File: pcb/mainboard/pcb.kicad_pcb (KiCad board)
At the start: 2 copper layers, 227 x 50 mm, 396 parts, among them J301 Conn_02x05_Odd_Even, J401 MICRO_SD(TFC-WPAPR-08), J501 Conn_01x40_MountingPin, J502 Conn_01x06_MountingPin, J503 Conn_01x40_MountingPin, J504 Conn_01x28_MountingPin, J601 USB_A, J602 USB_A, J603 USB_C_Receptacle_USB2.0, J604 USB_B_Micro, J701 Conn_01x02, J702 Conn_01x02, J703 AudioJack3_SwitchT, J800 Conn_01x28_MountingPin, Q1 FDMC8327L, Q2 FDMC8327L, Q3 2SK3018, U1 SY8120, U101 MCIMX7S5EVM08SC, U2 SY8120, U202 MT41K256M16HA, U203 MT41K256M16HA, U3 SY8120, U301 LPC5500_FBD64, U302 74LS154, U4 SY8120, U5 SY8120, U501 CAT4139, U502 SSD2828, U503 DS90C385A, U504 SM351LT, U6 SY8120, U601 USB2514B_Bi, U602 AP2171W, U603 AP2171W, U604 FUSB302BMPX, U605 USBLC6-2P6, U606 CP2102N-Axx-xQFN28, U7 LT8606, U701 WM8960, U8 LTC4162-F, U9 ADP123, U901 RTL8723BS, Y101 24MHz, Y102 32.768kHz, Y301 16MHz, Y501 24MHz, Y601 24MHz

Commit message: - pcb: components placed
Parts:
- removed C615, C616: 100nF, Capacitor_SMD:C_0402_1005Metric
- removed C617, C618: 10uF/6.3V, Capacitor_SMD:C_0603_1608Metric
- removed C701, C702, C703, C704: 1uF, Capacitor_SMD:C_0402_1005Metric
- removed D301: 1N5819, Diode_SMD:D_SOD-123
- removed D601, D602: LED, LED_SMD:LED_0603_1608Metric
- removed MK701, MK702: Microphone, Connector_PinSocket_1.27mm:PinSocket_1x02_P1.27mm_Vertical
- removed R303, R609, TH1: 10K, Resistor_SMD:R_0402_1005Metric
- removed R608: 100K, Resistor_SMD:R_0402_1005Metric
- removed R610: 20K, Resistor_SMD:R_0402_1005Metric
- removed R701, R702: 2.2K, Resistor_SMD:R_0402_1005Metric
- removed U606: CP2102N-Axx-xQFN28, Package_DFN_QFN:QFN-28-1EP_5x5mm_P0.5mm_EP3.35x3.35mm
- added C317: 100nF, Capacitor_SMD:C_0402_1005Metric, F.Cu at (99.1, 100.8)
- added C619: 10uF/6.3V, Capacitor_SMD:C_0603_1608Metric, F.Cu at (246.7, 97.3)
- added C620: 10uF/6.3V, Capacitor_SMD:C_0603_1608Metric, F.Cu at (246.5, 118.7)
- added C76: 220nF, Capacitor_SMD:C_0402_1005Metric, B.Cu at (144.3, 95.8)
- added C77: 2.2uF, Capacitor_SMD:C_0402_1005Metric, B.Cu at (142.2, 93.5)
- added C78: 220nF, Capacitor_SMD:C_0402_1005Metric, B.Cu at (143.8, 97.5)
- added C79: 220nF, Capacitor_SMD:C_0402_1005Metric, B.Cu at (144.1, 99.2)
- added C80: 2.2uF, Capacitor_SMD:C_0402_1005Metric, B.Cu at (145.2, 98.8)
- added C81: 1uF, Capacitor_SMD:C_0402_1005Metric, F.Cu at (63.5, 104.4)
- added J1: Conn_01x10_MountingPin, Connector_FFC-FPC:Hirose_FH12-10S-0.5SH_1x10-1MP_P0.50mm_Horizontal, F.Cu at (60.0, 83.0)
- added U1001: XC7A15T-FTG256, Package_BGA:Xilinx_FTG256, F.Cu at (203.9, 103.8)
- added U1002: MT41K64M16HA, Package_BGA:BGA-96_9.0x13.0mm_Layout2x3x16_P0.8mm, F.Cu at (185.7, 103.7)
- C10, C11, C12, C13, C14, C15, C16, C17, C18, C601, C603, C605, C606, C7, C8, C9: footprint Capacitor_SMD:C_0603_1608Metric -> Capacitor_SMD:C_0402_1005Metric
- C101, C102, C103, C104, C105, C106, C107, C108, C109, C110, C111, C114, C115, C117, C118, C119, C120, C122, C123, C124, C125, C126, L101, R115: moved to B.Cu
- J301: value Conn_02x05_Odd_Even -> Conn_01x06_MountingPin; footprint Connector_PinHeader_1.27mm:PinHeader_2x05_P1.27mm_Vertical_SMD -> Connector_FFC-FPC:Hirose_FH12-6S-0.5SH_1x06-1MP_P0.50mm_Horizontal
- J800: footprint Connector_FFC-FPC:Molex_200528-0280_1x28-1MP_P1.00mm_Horizontal -> Connector_FFC-FPC:TE_2-84953-8_1x28-1MP_P1.0mm_Horizontal
- R606, R607: value 1K -> 22
- moved L701 249.6 mm to (52.3, 101.8), turned to -90 degrees
- moved C709 246.9 mm to (53.4, 92.5), turned to 90 degrees
- moved L704 244.4 mm to (61.8, 94.5)
- moved C712 244.3 mm to (55.1, 90.7), turned to 90 degrees
- moved J701 243.4 mm to (58.9, 126.2), turned to 90 degrees
- moved C716 243.1 mm to (63.9, 96.3), turned to 90 degrees
- moved C714 242.8 mm to (63.9, 98.2), turned to 90 degrees
- moved C707 242.2 mm to (59.4, 92.5), turned to 90 degrees
- moved C706 241.5 mm to (55.4, 101.2), turned to -90 degrees
- moved L703 240.8 mm to (61.8, 92.9)
- moved C705 240.7 mm to (52.4, 98.9), turned to 180 degrees
- moved C715 240.5 mm to (52.9, 94.6), turned to 90 degrees
- moved C720 240.4 mm to (65.0, 96.9), turned to -90 degrees
- moved C708 237.3 mm to (61.2, 97.4)
- moved C710 237.2 mm to (52.0, 92.0), turned to 90 degrees
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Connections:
- net /ec/MPU_JTAG_TCK renamed /ec/EC_SWCLK
- net Net-(R20-Pad1) renamed /power/BAT_NTC
- C31 pad 1: +3V3 -> +5V
- C35 pad 1: +3V3 -> +5V
- C43 pad 1: +VCCIO_WL -> +VCCIO_SD
- C44 pad 1: +VCCIO_WL -> +VCCIO_SD
- J301 pad 2: /ec/MPU_JTAG_TMS -> (no net)
- J301 pad 3: GND -> (no net)
- J301 pad 5: GND -> /ec/EC_SWDIO
- J301 pad 6: /ec/MPU_JTAG_TDO -> GND
- J401 pad 9: unconnected-(J401-Pad9) -> (no net)
- J501 pad 20: unconnected-(J501-Pad20) -> (no net)
- J501 pad 21: unconnected-(J501-Pad21) -> (no net)
- J501 pad 22: unconnected-(J501-Pad22) -> (no net)
- J501 pad 23: unconnected-(J501-Pad23) -> (no net)
- J501 pad 25: unconnected-(J501-Pad25) -> (no net)
- J501 pad 26: unconnected-(J501-Pad26) -> (no net)
- J501 pad 31: unconnected-(J501-Pad31) -> (no net)
- J501 pad 34: unconnected-(J501-Pad34) -> (no net)
- J501 pad 40: unconnected-(J501-Pad40) -> (no net)
- J502 pad 5: LCD_TP_INT -> (no net)
- J603 pad A8: unconnected-(J603-PadA8) -> (no net)
- J603 pad B8: unconnected-(J603-PadB8) -> (no net)
- J604 pad 1: Net-(C616-Pad1) -> (no net)
- J800 pad 1: KSO0 -> GND
- J800 pad 10: KSO5 -> KSO10
- J800 pad 11: KSI4 -> KSO9
- J800 pad 12: KSI5 -> KSO8
- J800 pad 13: KSO6 -> KSO7
- J800 pad 14: KSI6 -> KSI7
- J800 pad 15: KSI7 -> KSI6
- J800 pad 16: KSO7 -> KSO6
- J800 pad 17: KSO8 -> KSI5
- J800 pad 18: KSO9 -> KSI4
- J800 pad 19: KSO10 -> KSO5
- J800 pad 2: KSI0 -> (no net)
- J800 pad 20: KSO11 -> KSI3
- J800 pad 21: KSO12 -> KSO4
- J800 pad 22: KSO1 -> KSI2
- J800 pad 23: KSO13 -> KSO3
- J800 pad 24: KSO14 -> KSI1
- J800 pad 25: KSO3 -> KSO2
- J800 pad 26: KSO15 -> KSO1
- J800 pad 27: KBD_DET -> KSI0
- J800 pad 28: GND -> KSO0
- J800 pad 3: KSO1 -> KSO15
- J800 pad 4: KSO2 -> KSO3
- J800 pad 5: KSI1 -> KSO14
- J800 pad 6: KSO3 -> KSO13
- J800 pad 7: KSI2 -> KSO1
- J800 pad 8: KSO4 -> KSO12
- J800 pad 9: KSI3 -> KSO11
- R101 pad 2: +RTC -> +3V3_SB
- R103 pad 2: +RTC -> +3V3_SB
- R17 pad 1: +VCCIO_WL -> +VCCIO_SD
- R24 pad 1: +VCCIO_WL -> +VCCIO_SD
- R606 pad 1: Net-(D601-Pad2) -> Net-(J604-Pad3)
- R606 pad 2: Net-(C615-Pad1) -> DEBUG_USB_DP
- R607 pad 1: Net-(D602-Pad2) -> Net-(J604-Pad2)
- R607 pad 2: Net-(C615-Pad1) -> DEBUG_USB_DM
- R708 pad 1: +3.3VA -> (no net)
- RN101 pad 1: unconnected-(RN101-Pad1) -> (no net)
- U1 pad 4: 5V_EN -> (no net)
- U101 pad A12: unconnected-(U101-PadA12) -> (no net)
- U101 pad A14: unconnected-(U101-PadA14) -> (no net)
- U101 pad A15: unconnected-(U101-PadA15) -> (no net)
- U101 pad A16: unconnected-(U101-PadA16) -> (no net)
- U101 pad A18: unconnected-(U101-PadA18) -> (no net)
- U101 pad A19: unconnected-(U101-PadA19) -> (no net)
- U101 pad A2: unconnected-(U101-PadA2) -> (no net)
- U101 pad A20: unconnected-(U101-PadA20) -> (no net)
- U101 pad AA10: GND -> Net-(C65-Pad2)
- U101 pad AA11: GND -> Net-(C65-Pad2)
- U101 pad AA12: GND -> Net-(C65-Pad2)
- U101 pad AA14: unconnected-(U101-PadAA14) -> (no net)
- U101 pad AA22: unconnected-(U101-PadAA22) -> (no net)
- U101 pad AA3: unconnected-(U101-PadAA3) -> (no net)
- U101 pad AA4: unconnected-(U101-PadAA4) -> (no net)
- U101 pad AA5: unconnected-(U101-PadAA5) -> (no net)
- U101 pad AA7: unconnected-(U101-PadAA7) -> (no net)
- U101 pad AB10: unconnected-(U101-PadAB10) -> (no net)
- U101 pad AB11: unconnected-(U101-PadAB11) -> (no net)
- U101 pad AB20: unconnected-(U101-PadAB20) -> (no net)
- U101 pad AB22: unconnected-(U101-PadAB22) -> (no net)
- U101 pad AB6: unconnected-(U101-PadAB6) -> (no net)
- U101 pad AC10: unconnected-(U101-PadAC10) -> (no net)
- U101 pad AC11: unconnected-(U101-PadAC11) -> (no net)
- U101 pad AC8: PB_STAT -> (no net)
- U101 pad AD10: unconnected-(U101-PadAD10) -> (no net)
- U101 pad AD11: unconnected-(U101-PadAD11) -> (no net)
- U101 pad AD4: unconnected-(U101-PadAD4) -> (no net)
- U101 pad AE10: unconnected-(U101-PadAE10) -> (no net)
- U101 pad AE11: unconnected-(U101-PadAE11) -> (no net)
- U101 pad B1: unconnected-(U101-PadB1) -> (no net)
- U101 pad B12: unconnected-(U101-PadB12) -> (no net)
- U101 pad B14: unconnected-(U101-PadB14) -> (no net)
- U101 pad B15: unconnected-(U101-PadB15) -> (no net)
- U101 pad B16: unconnected-(U101-PadB16) -> (no net)
- U101 pad B18: unconnected-(U101-PadB18) -> (no net)
- U101 pad B19: unconnected-(U101-PadB19) -> (no net)
- U101 pad B2: unconnected-(U101-PadB2) -> (no net)
- U101 pad B20: unconnected-(U101-PadB20) -> (no net)
- U101 pad B4: unconnected-(U101-PadB4) -> (no net)
- U101 pad C1: unconnected-(U101-PadC1) -> (no net)
- U101 pad C10: USB_HOST_VBUS -> (no net)
- U101 pad C12: unconnected-(U101-PadC12) -> (no net)
- U101 pad C2: unconnected-(U101-PadC2) -> (no net)
- U101 pad C3: unconnected-(U101-PadC3) -> (no net)
- U101 pad C6: unconnected-(U101-PadC6) -> (no net)
- U101 pad C7: unconnected-(U101-PadC7) -> (no net)
- U101 pad C8: USB_OTG_VBUS -> (no net)
- U101 pad D12: unconnected-(U101-PadD12) -> (no net)
- U101 pad D15: unconnected-(U101-PadD15) -> (no net)
- U101 pad D16: unconnected-(U101-PadD16) -> (no net)
- U101 pad D19: unconnected-(U101-PadD19) -> (no net)
- U101 pad D3: unconnected-(U101-PadD3) -> (no net)
- U101 pad D8: unconnected-(U101-PadD8) -> (no net)
- U101 pad D9: unconnected-(U101-PadD9) -> (no net)
- U101 pad E1: unconnected-(U101-PadE1) -> (no net)
- U101 pad E14: unconnected-(U101-PadE14) -> (no net)
- U101 pad E15: unconnected-(U101-PadE15) -> (no net)
- U101 pad E16: unconnected-(U101-PadE16) -> (no net)
- U101 pad E17: unconnected-(U101-PadE17) -> (no net)
- U101 pad E18: unconnected-(U101-PadE18) -> (no net)
- U101 pad E19: unconnected-(U101-PadE19) -> (no net)
- U101 pad E2: unconnected-(U101-PadE2) -> (no net)
- U101 pad E8: unconnected-(U101-PadE8) -> (no net)
- U101 pad E9: unconnected-(U101-PadE9) -> (no net)
- U101 pad F1: unconnected-(U101-PadF1) -> (no net)
- U101 pad F15: unconnected-(U101-PadF15) -> (no net)
- U101 pad F16: unconnected-(U101-PadF16) -> (no net)
- U101 pad F17: unconnected-(U101-PadF17) -> (no net)
- U101 pad F2: unconnected-(U101-PadF2) -> (no net)
- U101 pad G1: unconnected-(U101-PadG1) -> (no net)
- U101 pad G2: unconnected-(U101-PadG2) -> (no net)
- U101 pad G24: unconnected-(U101-PadG24) -> (no net)
- U101 pad G3: unconnected-(U101-PadG3) -> (no net)
- U101 pad G5: unconnected-(U101-PadG5) -> (no net)
- U101 pad G6: unconnected-(U101-PadG6) -> (no net)
- U101 pad H14: unconnected-(U101-PadH14) -> (no net)
- U101 pad H20: unconnected-(U101-PadH20) -> (no net)
- U101 pad H22: unconnected-(U101-PadH22) -> (no net)
- U101 pad H23: unconnected-(U101-PadH23) -> (no net)
- U101 pad H24: unconnected-(U101-PadH24) -> (no net)
- U101 pad H3: unconnected-(U101-PadH3) -> (no net)
- U101 pad H4: unconnected-(U101-PadH4) -> (no net)
- U101 pad H5: unconnected-(U101-PadH5) -> (no net)
- U101 pad H6: unconnected-(U101-PadH6) -> (no net)
- U101 pad J1: unconnected-(U101-PadJ1) -> (no net)
- U101 pad J13: unconnected-(U101-PadJ13) -> Net-(U101-PadJ13)
- U101 pad J15: unconnected-(U101-PadJ15) -> Net-(C65-Pad2)
- U101 pad J17: unconnected-(U101-PadJ17) -> Net-(C65-Pad2)
- U101 pad J5: unconnected-(U101-PadJ5) -> (no net)
- U101 pad J6: unconnected-(U101-PadJ6) -> (no net)
- U101 pad K21: unconnected-(U101-PadK21) -> (no net)
- U101 pad K23: unconnected-(U101-PadK23) -> (no net)
- U101 pad K5: unconnected-(U101-PadK5) -> (no net)
- U101 pad K6: unconnected-(U101-PadK6) -> (no net)
- U101 pad L1: unconnected-(U101-PadL1) -> (no net)
- U101 pad L2: unconnected-(U101-PadL2) -> (no net)
- U101 pad L5: unconnected-(U101-PadL5) -> (no net)
- U101 pad L6: unconnected-(U101-PadL6) -> (no net)
- U101 pad M6: UART3_CTS -> (no net)
- U101 pad N1: unconnected-(U101-PadN1) -> (no net)
- U101 pad N3: unconnected-(U101-PadN3) -> (no net)
- U101 pad N5: unconnected-(U101-PadN5) -> (no net)
- U101 pad N6: unconnected-(U101-PadN6) -> (no net)
- U101 pad P1: unconnected-(U101-PadP1) -> (no net)
- U101 pad P2: unconnected-(U101-PadP2) -> (no net)
- U101 pad P3: unconnected-(U101-PadP3) -> (no net)
- U101 pad R2: unconnected-(U101-PadR2) -> (no net)
- U101 pad R5: unconnected-(U101-PadR5) -> (no net)
- U101 pad U2: /cpu/MPU_JTAG_TRST -> (no net)
- U101 pad U3: /cpu/MPU_JTAG_TDI -> (no net)
- U101 pad U4: /cpu/MPU_JTAG_TMS -> (no net)
- U101 pad U5: /cpu/MPU_JTAG_TCK -> (no net)
- U101 pad U6: /cpu/MPU_JTAG_TDO -> (no net)
- U101 pad U9: unconnected-(U101-PadU9) -> (no net)
- U101 pad V4: unconnected-(U101-PadV4) -> (no net)
- U101 pad Y1: unconnected-(U101-PadY1) -> (no net)
- U101 pad Y10: GND -> Net-(U101-PadJ13)
- U101 pad Y11: GND -> Net-(U101-PadJ13)
- U101 pad Y12: GND -> Net-(U101-PadJ13)
- U101 pad Y2: unconnected-(U101-PadY2) -> (no net)
- U101 pad Y3: unconnected-(U101-PadY3) -> (no net)
- U101 pad Y4: unconnected-(U101-PadY4) -> (no net)
- U101 pad Y5: unconnected-(U101-PadY5) -> (no net)
- U101 pad Y7: unconnected-(U101-PadY7) -> (no net)
- U101 pad Y8: unconnected-(U101-PadY8) -> (no net)
- U101 pad Y9: unconnected-(U101-PadY9) -> Net-(U101-PadJ13)
- U202 pad M7: unconnected-(U202-PadM7) -> (no net)
- U203 pad M7: unconnected-(U203-PadM7) -> (no net)
- U301 pad 12: unconnected-(U301-Pad12) -> (no net)
- U301 pad 15: unconnected-(U301-Pad15) -> (no net)
- U301 pad 18: unconnected-(U301-Pad18) -> (no net)
- U301 pad 21: POR -> SB_PG
- U301 pad 3: unconnected-(U301-Pad3) -> (no net)
- U301 pad 34: unconnected-(U301-Pad34) -> (no net)
- U301 pad 35: unconnected-(U301-Pad35) -> (no net)
- U301 pad 40: unconnected-(U301-Pad40) -> (no net)
- U301 pad 45: unconnected-(U301-Pad45) -> (no net)
- U301 pad 5: /ec/MPU_JTAG_TMS -> /ec/EC_SWDIO
- U301 pad 51: unconnected-(U301-Pad51) -> (no net)
- U301 pad 59: unconnected-(U301-Pad59) -> UART1_TXD
- U301 pad 60: unconnected-(U301-Pad60) -> UART1_RXD
- U301 pad 62: unconnected-(U301-Pad62) -> DEBUG_USB_DP
- U301 pad 63: unconnected-(U301-Pad63) -> DEBUG_USB_DM
- U301 pad 7: unconnected-(U301-Pad7) -> (no net)
- U502 pad 19: unconnected-(U502-Pad19) -> (no net)
- U502 pad 20: unconnected-(U502-Pad20) -> (no net)
- U502 pad 21: unconnected-(U502-Pad21) -> (no net)
- U502 pad 23: SPI_LCD_MISO -> (no net)
- U502 pad 24: SPI_LCD_MOSI -> (no net)
- U502 pad 25: SPI_LCD_SCLK -> (no net)
- U502 pad 26: unconnected-(U502-Pad26) -> (no net)
- U502 pad 59: SPI_LCD_CS -> (no net)
- U502 pad 61: unconnected-(U502-Pad61) -> (no net)
- U504 pad 2: LCD_LID -> (no net)
- U601 pad 18: unconnected-(U601-Pad18) -> (no net)
- U601 pad 19: unconnected-(U601-Pad19) -> (no net)
- U601 pad 20: unconnected-(U601-Pad20) -> (no net)
- U601 pad 21: unconnected-(U601-Pad21) -> (no net)
- U601 pad 22: unconnected-(U601-Pad22) -> (no net)
- U601 pad 8: unconnected-(U601-Pad8) -> (no net)
- U601 pad 9: unconnected-(U601-Pad9) -> (no net)
- U604 pad 5: unconnected-(U604-Pad5) -> (no net)
- U7 pad 5: unconnected-(U7-Pad5) -> (no net)
- U701 pad 2: unconnected-(U701-Pad2) -> (no net)
- U701 pad 3: Net-(C701-Pad1) -> (no net)
- U701 pad 30: unconnected-(U701-Pad30) -> (no net)
- U701 pad 4: Net-(C702-Pad1) -> (no net)
- U701 pad 5: Net-(C704-Pad1) -> (no net)
- U701 pad 6: Net-(C703-Pad1) -> (no net)
- U9 pad 1: +3V3 -> +5V
- U9 pad 3: +3V3 -> +5V
- U9 pad 5: +VCCIO_WL -> +VCCIO_SD
- U901 pad 10: unconnected-(U901-Pad10) -> (no net)
- U901 pad 11: unconnected-(U901-Pad11) -> (no net)
- U901 pad 21: unconnected-(U901-Pad21) -> (no net)
- U901 pad 23: unconnected-(U901-Pad23) -> (no net)
- U901 pad 25: unconnected-(U901-Pad25) -> (no net)
- U901 pad 26: unconnected-(U901-Pad26) -> (no net)
- U901 pad 27: unconnected-(U901-Pad27) -> (no net)
- U901 pad 28: unconnected-(U901-Pad28) -> (no net)
- U901 pad 29: unconnected-(U901-Pad29) -> (no net)
- U901 pad 3: unconnected-(U901-Pad3) -> (no net)
- U901 pad 30: unconnected-(U901-Pad30) -> (no net)
- U901 pad 32: unconnected-(U901-Pad32) -> (no net)
- U901 pad 35: unconnected-(U901-Pad35) -> (no net)
- U901 pad 37: unconnected-(U901-Pad37) -> (no net)
- U901 pad 38: unconnected-(U901-Pad38) -> (no net)
- U901 pad 39: unconnected-(U901-Pad39) -> (no net)
- U901 pad 4: unconnected-(U901-Pad4) -> (no net)
- U901 pad 40: unconnected-(U901-Pad40) -> (no net)
- U901 pad 5: unconnected-(U901-Pad5) -> (no net)
- U901 pad 8: unconnected-(U901-Pad8) -> (no net)
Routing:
- net Net-(U101-PadJ13): track 0.00 -> 2.12 mm, vias 0 -> 2
- net Net-(C65-Pad2): track 0.53 -> 2.12 mm, vias 1 -> 3
- net +1V0: track 11.7 -> 12.4 mm
- net Net-(C66-Pad2): track 0.53 -> 1.27 mm
- net GND: track 61.6 -> 61.4 mm, vias 110 -> 100
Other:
- outline, holes or cut-outs redrawn
- board text added: "Reserved Area for M.2 SSD"
- board text added: "Reserved Area for {dblquote}Caster{dblquote} EPDC"

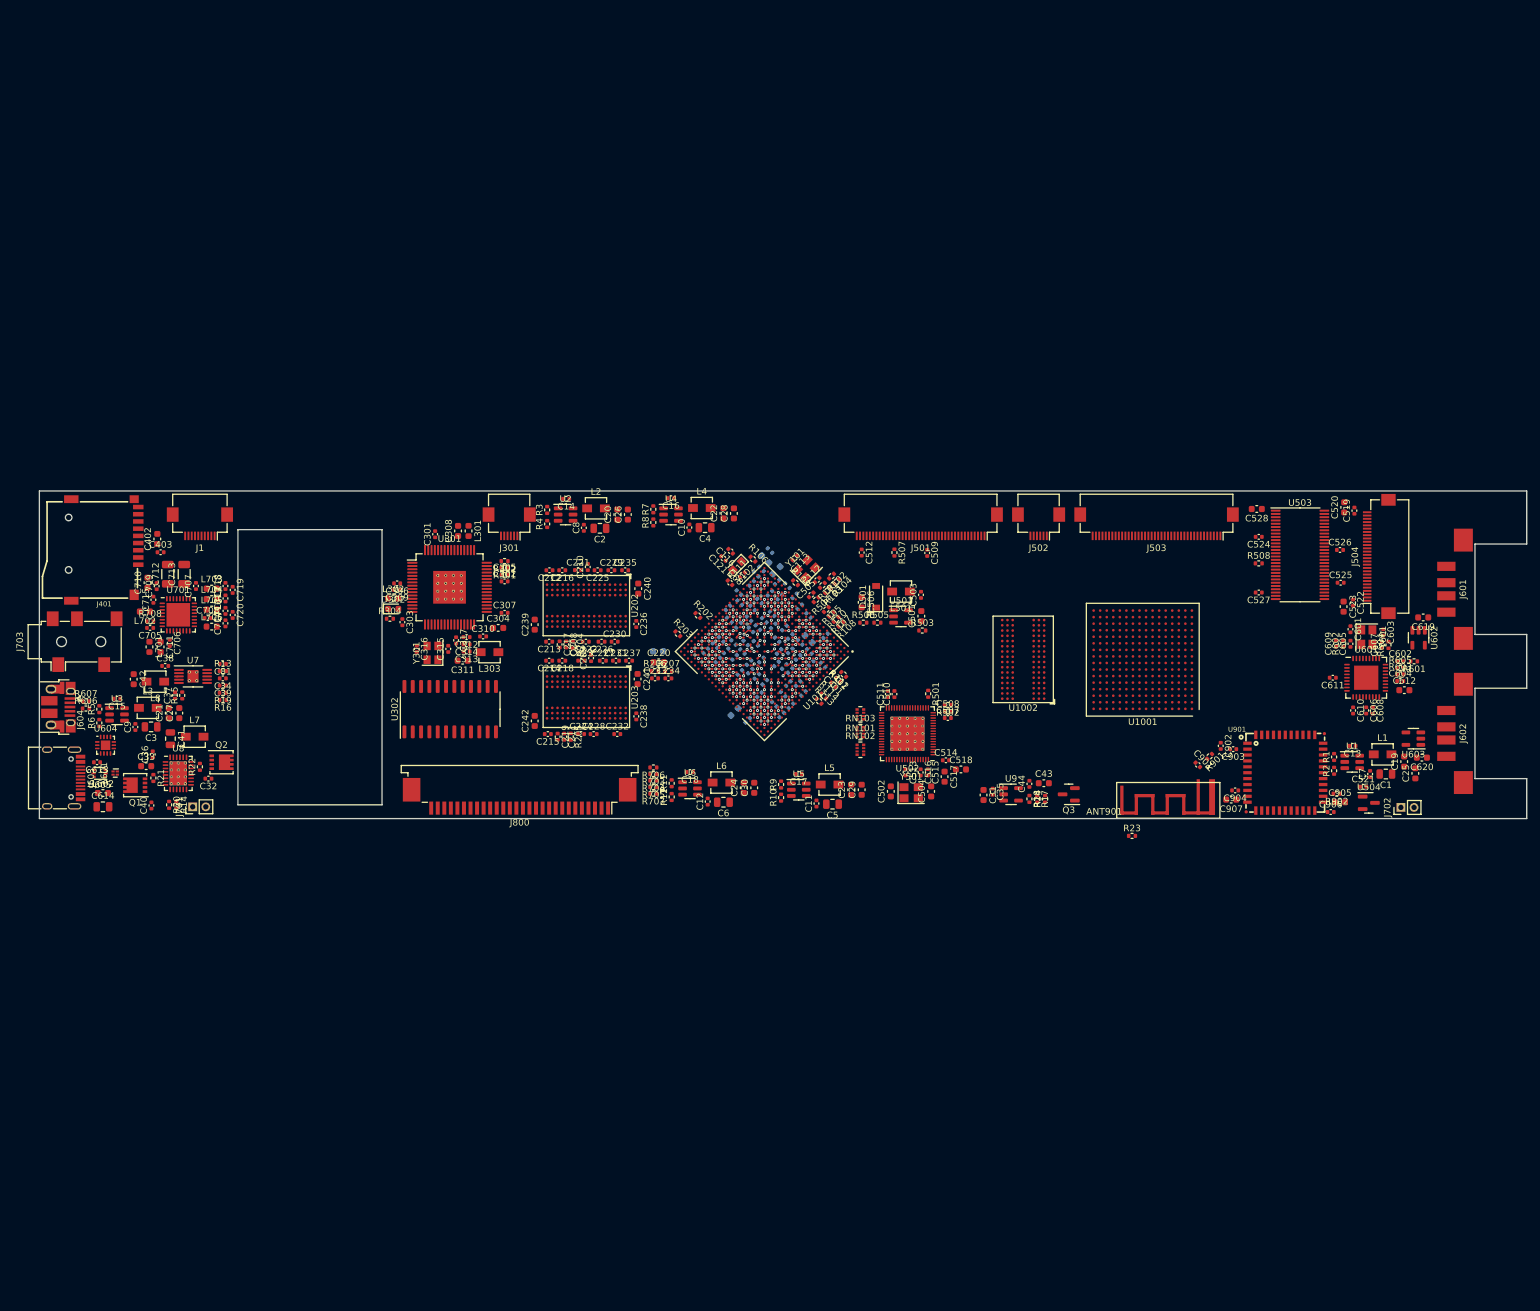
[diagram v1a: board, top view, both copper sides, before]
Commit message: - pcb: ddr layout
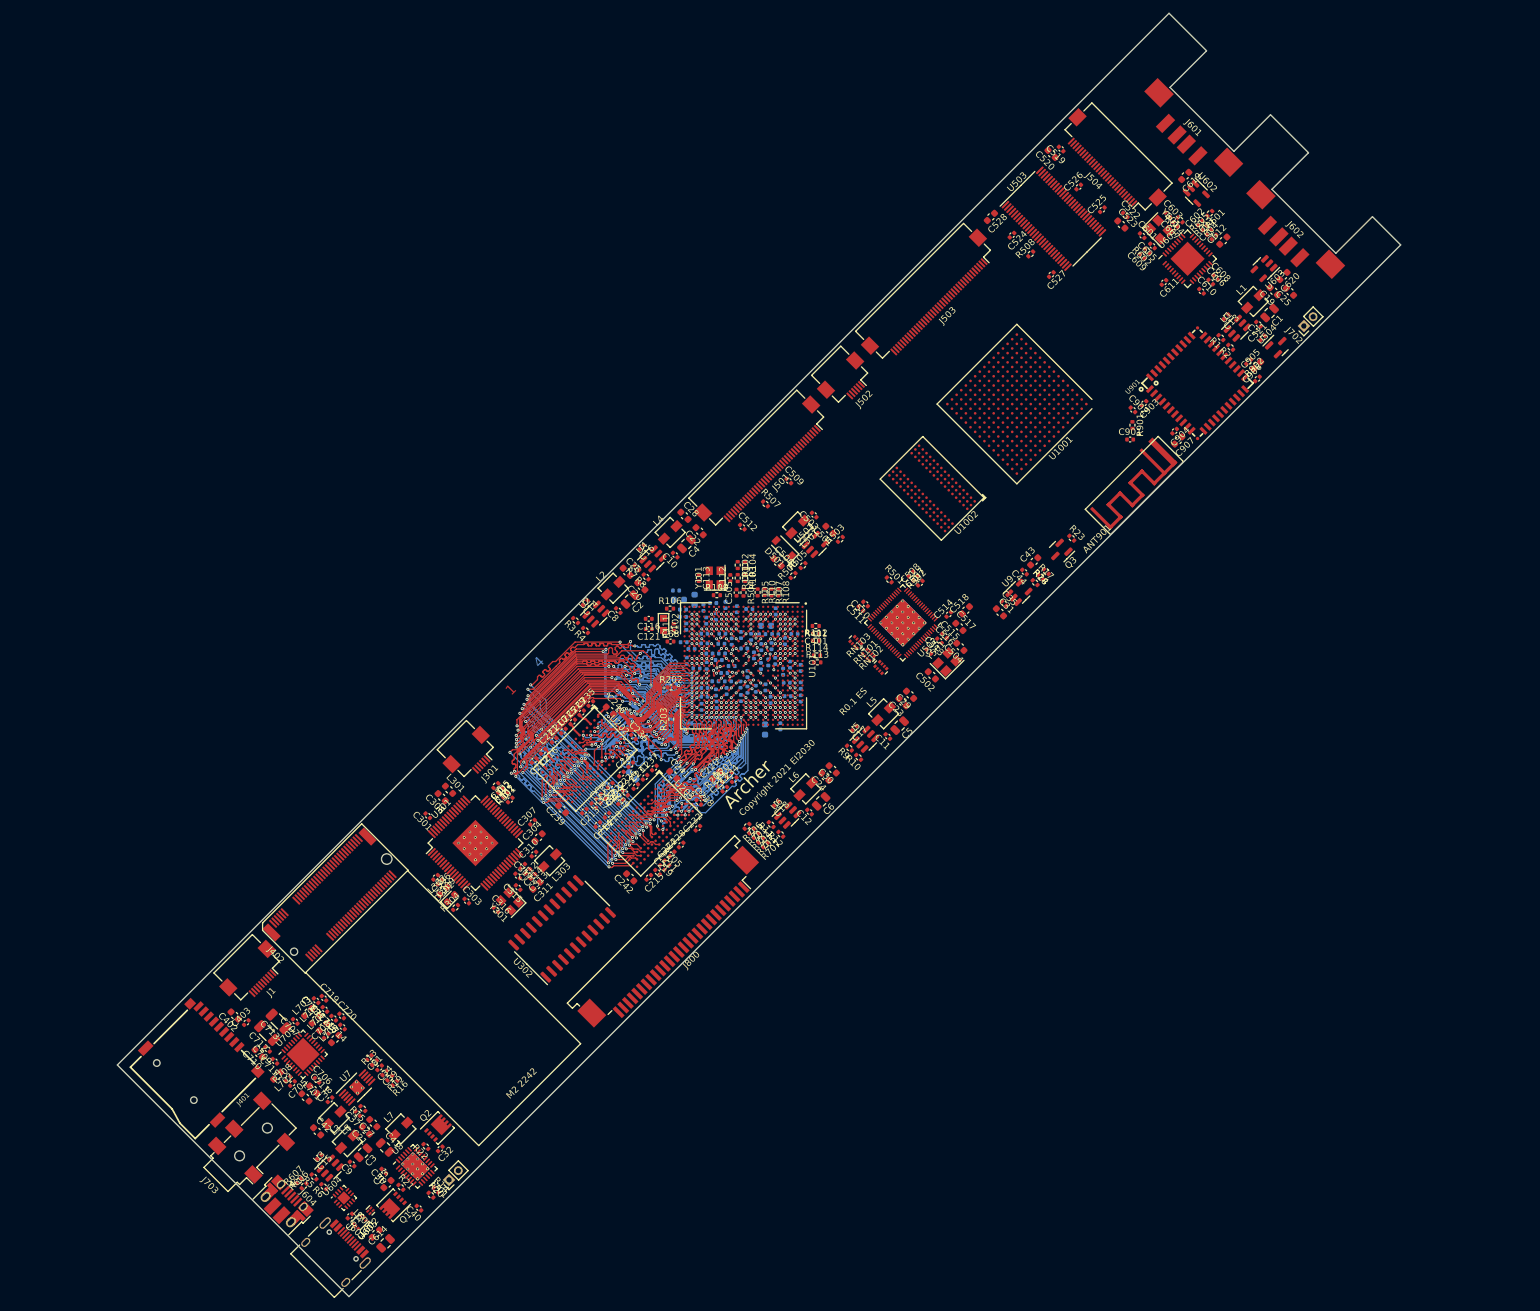
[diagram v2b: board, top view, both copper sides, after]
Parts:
- added J402: Bus_M.2_Socket_B, footprints:M2_BKEY, F.Cu at (80.4, 140.2)
- U1001: value XC7A15T-FTG256 -> DNP/XC7A15T-FTG256
- U1002: value MT41K64M16HA -> DNP/MT41K64M16HA
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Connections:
- U1001 pad A1: unconnected-(U1001-PadA1) -> (no net)
- U1001 pad A10: unconnected-(U1001-PadA10) -> (no net)
- U1001 pad A11: unconnected-(U1001-PadA11) -> (no net)
- U1001 pad A12: unconnected-(U1001-PadA12) -> (no net)
- U1001 pad A13: unconnected-(U1001-PadA13) -> (no net)
- U1001 pad A14: unconnected-(U1001-PadA14) -> (no net)
- U1001 pad A15: unconnected-(U1001-PadA15) -> (no net)
- U1001 pad A16: unconnected-(U1001-PadA16) -> (no net)
- U1001 pad A2: unconnected-(U1001-PadA2) -> (no net)
- U1001 pad A3: unconnected-(U1001-PadA3) -> (no net)
- U1001 pad A4: unconnected-(U1001-PadA4) -> (no net)
- U1001 pad A5: unconnected-(U1001-PadA5) -> (no net)
- U1001 pad A6: unconnected-(U1001-PadA6) -> (no net)
- U1001 pad A7: unconnected-(U1001-PadA7) -> (no net)
- U1001 pad A8: unconnected-(U1001-PadA8) -> (no net)
- U1001 pad A9: unconnected-(U1001-PadA9) -> (no net)
- U1001 pad B1: unconnected-(U1001-PadB1) -> (no net)
- U1001 pad B10: unconnected-(U1001-PadB10) -> (no net)
- U1001 pad B11: unconnected-(U1001-PadB11) -> (no net)
- U1001 pad B12: unconnected-(U1001-PadB12) -> (no net)
- U1001 pad B13: unconnected-(U1001-PadB13) -> (no net)
- U1001 pad B14: unconnected-(U1001-PadB14) -> (no net)
- U1001 pad B15: unconnected-(U1001-PadB15) -> (no net)
- U1001 pad B16: unconnected-(U1001-PadB16) -> (no net)
- U1001 pad B2: unconnected-(U1001-PadB2) -> (no net)
- U1001 pad B3: unconnected-(U1001-PadB3) -> (no net)
- U1001 pad B4: unconnected-(U1001-PadB4) -> (no net)
- U1001 pad B5: unconnected-(U1001-PadB5) -> (no net)
- U1001 pad B6: unconnected-(U1001-PadB6) -> (no net)
- U1001 pad B7: unconnected-(U1001-PadB7) -> (no net)
- U1001 pad B8: unconnected-(U1001-PadB8) -> (no net)
- U1001 pad B9: unconnected-(U1001-PadB9) -> (no net)
- U1001 pad C1: unconnected-(U1001-PadC1) -> (no net)
- U1001 pad C10: unconnected-(U1001-PadC10) -> (no net)
- U1001 pad C11: unconnected-(U1001-PadC11) -> (no net)
- U1001 pad C12: unconnected-(U1001-PadC12) -> (no net)
- U1001 pad C13: unconnected-(U1001-PadC13) -> (no net)
- U1001 pad C14: unconnected-(U1001-PadC14) -> (no net)
- U1001 pad C15: unconnected-(U1001-PadC15) -> (no net)
- U1001 pad C16: unconnected-(U1001-PadC16) -> (no net)
- U1001 pad C2: unconnected-(U1001-PadC2) -> (no net)
- U1001 pad C3: unconnected-(U1001-PadC3) -> (no net)
- U1001 pad C4: unconnected-(U1001-PadC4) -> (no net)
- U1001 pad C5: unconnected-(U1001-PadC5) -> (no net)
- U1001 pad C6: unconnected-(U1001-PadC6) -> (no net)
- U1001 pad C7: unconnected-(U1001-PadC7) -> (no net)
- U1001 pad C8: unconnected-(U1001-PadC8) -> (no net)
- U1001 pad C9: unconnected-(U1001-PadC9) -> (no net)
- U1001 pad D1: unconnected-(U1001-PadD1) -> (no net)
- U1001 pad D10: unconnected-(U1001-PadD10) -> (no net)
- U1001 pad D11: unconnected-(U1001-PadD11) -> (no net)
- U1001 pad D12: unconnected-(U1001-PadD12) -> (no net)
- U1001 pad D13: unconnected-(U1001-PadD13) -> (no net)
- U1001 pad D14: unconnected-(U1001-PadD14) -> (no net)
- U1001 pad D15: unconnected-(U1001-PadD15) -> (no net)
- U1001 pad D16: unconnected-(U1001-PadD16) -> (no net)
- U1001 pad D2: unconnected-(U1001-PadD2) -> (no net)
- U1001 pad D3: unconnected-(U1001-PadD3) -> (no net)
- U1001 pad D4: unconnected-(U1001-PadD4) -> (no net)
- U1001 pad D5: unconnected-(U1001-PadD5) -> (no net)
- U1001 pad D6: unconnected-(U1001-PadD6) -> (no net)
- U1001 pad D7: unconnected-(U1001-PadD7) -> (no net)
- U1001 pad D8: unconnected-(U1001-PadD8) -> (no net)
- U1001 pad D9: unconnected-(U1001-PadD9) -> (no net)
- U1001 pad E1: unconnected-(U1001-PadE1) -> (no net)
- U1001 pad E10: unconnected-(U1001-PadE10) -> (no net)
- U1001 pad E11: unconnected-(U1001-PadE11) -> (no net)
- U1001 pad E12: unconnected-(U1001-PadE12) -> (no net)
- U1001 pad E13: unconnected-(U1001-PadE13) -> (no net)
- U1001 pad E14: unconnected-(U1001-PadE14) -> (no net)
- U1001 pad E15: unconnected-(U1001-PadE15) -> (no net)
- U1001 pad E16: unconnected-(U1001-PadE16) -> (no net)
- U1001 pad E2: unconnected-(U1001-PadE2) -> (no net)
- U1001 pad E3: unconnected-(U1001-PadE3) -> (no net)
- U1001 pad E4: unconnected-(U1001-PadE4) -> (no net)
- U1001 pad E5: unconnected-(U1001-PadE5) -> (no net)
- U1001 pad E6: unconnected-(U1001-PadE6) -> (no net)
- U1001 pad E7: unconnected-(U1001-PadE7) -> (no net)
- U1001 pad E8: unconnected-(U1001-PadE8) -> (no net)
- U1001 pad E9: unconnected-(U1001-PadE9) -> (no net)
- U1001 pad F1: unconnected-(U1001-PadF1) -> (no net)
- U1001 pad F10: unconnected-(U1001-PadF10) -> (no net)
- U1001 pad F11: unconnected-(U1001-PadF11) -> (no net)
- U1001 pad F12: unconnected-(U1001-PadF12) -> (no net)
- U1001 pad F13: unconnected-(U1001-PadF13) -> (no net)
- U1001 pad F14: unconnected-(U1001-PadF14) -> (no net)
- U1001 pad F15: unconnected-(U1001-PadF15) -> (no net)
- U1001 pad F16: unconnected-(U1001-PadF16) -> (no net)
- U1001 pad F2: unconnected-(U1001-PadF2) -> (no net)
- U1001 pad F3: unconnected-(U1001-PadF3) -> (no net)
- U1001 pad F4: unconnected-(U1001-PadF4) -> (no net)
- U1001 pad F5: unconnected-(U1001-PadF5) -> (no net)
- U1001 pad F6: unconnected-(U1001-PadF6) -> (no net)
- U1001 pad F7: unconnected-(U1001-PadF7) -> (no net)
- U1001 pad F8: unconnected-(U1001-PadF8) -> (no net)
- U1001 pad F9: unconnected-(U1001-PadF9) -> (no net)
- U1001 pad G1: unconnected-(U1001-PadG1) -> (no net)
- U1001 pad G10: unconnected-(U1001-PadG10) -> (no net)
- U1001 pad G11: unconnected-(U1001-PadG11) -> (no net)
- U1001 pad G12: unconnected-(U1001-PadG12) -> (no net)
- U1001 pad G13: unconnected-(U1001-PadG13) -> (no net)
- U1001 pad G14: unconnected-(U1001-PadG14) -> (no net)
- U1001 pad G15: unconnected-(U1001-PadG15) -> (no net)
- U1001 pad G16: unconnected-(U1001-PadG16) -> (no net)
- U1001 pad G2: unconnected-(U1001-PadG2) -> (no net)
- U1001 pad G3: unconnected-(U1001-PadG3) -> (no net)
- U1001 pad G4: unconnected-(U1001-PadG4) -> (no net)
- U1001 pad G5: unconnected-(U1001-PadG5) -> (no net)
- U1001 pad G6: unconnected-(U1001-PadG6) -> (no net)
- U1001 pad G7: unconnected-(U1001-PadG7) -> (no net)
- U1001 pad G8: unconnected-(U1001-PadG8) -> (no net)
- U1001 pad G9: unconnected-(U1001-PadG9) -> (no net)
- U1001 pad H1: unconnected-(U1001-PadH1) -> (no net)
- U1001 pad H10: unconnected-(U1001-PadH10) -> (no net)
- U1001 pad H11: unconnected-(U1001-PadH11) -> (no net)
- U1001 pad H12: unconnected-(U1001-PadH12) -> (no net)
- U1001 pad H13: unconnected-(U1001-PadH13) -> (no net)
- U1001 pad H14: unconnected-(U1001-PadH14) -> (no net)
- U1001 pad H15: unconnected-(U1001-PadH15) -> (no net)
- U1001 pad H16: unconnected-(U1001-PadH16) -> (no net)
- U1001 pad H2: unconnected-(U1001-PadH2) -> (no net)
- U1001 pad H3: unconnected-(U1001-PadH3) -> (no net)
- U1001 pad H4: unconnected-(U1001-PadH4) -> (no net)
- U1001 pad H5: unconnected-(U1001-PadH5) -> (no net)
- U1001 pad H6: unconnected-(U1001-PadH6) -> (no net)
- U1001 pad H7: unconnected-(U1001-PadH7) -> (no net)
- U1001 pad H8: unconnected-(U1001-PadH8) -> (no net)
- U1001 pad H9: unconnected-(U1001-PadH9) -> (no net)
- U1001 pad J1: unconnected-(U1001-PadJ1) -> (no net)
- U1001 pad J10: unconnected-(U1001-PadJ10) -> (no net)
- U1001 pad J11: unconnected-(U1001-PadJ11) -> (no net)
- U1001 pad J12: unconnected-(U1001-PadJ12) -> (no net)
- U1001 pad J13: unconnected-(U1001-PadJ13) -> (no net)
- U1001 pad J14: unconnected-(U1001-PadJ14) -> (no net)
- U1001 pad J15: unconnected-(U1001-PadJ15) -> (no net)
- U1001 pad J16: unconnected-(U1001-PadJ16) -> (no net)
- U1001 pad J2: unconnected-(U1001-PadJ2) -> (no net)
- U1001 pad J3: unconnected-(U1001-PadJ3) -> (no net)
- U1001 pad J4: unconnected-(U1001-PadJ4) -> (no net)
- U1001 pad J5: unconnected-(U1001-PadJ5) -> (no net)
- U1001 pad J6: unconnected-(U1001-PadJ6) -> (no net)
- U1001 pad J7: unconnected-(U1001-PadJ7) -> (no net)
- U1001 pad J8: unconnected-(U1001-PadJ8) -> (no net)
- U1001 pad J9: unconnected-(U1001-PadJ9) -> (no net)
- U1001 pad K1: unconnected-(U1001-PadK1) -> (no net)
- U1001 pad K10: unconnected-(U1001-PadK10) -> (no net)
- U1001 pad K11: unconnected-(U1001-PadK11) -> (no net)
- U1001 pad K12: unconnected-(U1001-PadK12) -> (no net)
- U1001 pad K13: unconnected-(U1001-PadK13) -> (no net)
- U1001 pad K14: unconnected-(U1001-PadK14) -> (no net)
- U1001 pad K15: unconnected-(U1001-PadK15) -> (no net)
- U1001 pad K16: unconnected-(U1001-PadK16) -> (no net)
- U1001 pad K2: unconnected-(U1001-PadK2) -> (no net)
- U1001 pad K3: unconnected-(U1001-PadK3) -> (no net)
- U1001 pad K4: unconnected-(U1001-PadK4) -> (no net)
- U1001 pad K5: unconnected-(U1001-PadK5) -> (no net)
- U1001 pad K6: unconnected-(U1001-PadK6) -> (no net)
- U1001 pad K7: unconnected-(U1001-PadK7) -> (no net)
- U1001 pad K8: unconnected-(U1001-PadK8) -> (no net)
- U1001 pad K9: unconnected-(U1001-PadK9) -> (no net)
- U1001 pad L1: unconnected-(U1001-PadL1) -> (no net)
- U1001 pad L10: unconnected-(U1001-PadL10) -> (no net)
- U1001 pad L11: unconnected-(U1001-PadL11) -> (no net)
- U1001 pad L12: unconnected-(U1001-PadL12) -> (no net)
- U1001 pad L13: unconnected-(U1001-PadL13) -> (no net)
- U1001 pad L14: unconnected-(U1001-PadL14) -> (no net)
- U1001 pad L15: unconnected-(U1001-PadL15) -> (no net)
- U1001 pad L16: unconnected-(U1001-PadL16) -> (no net)
- U1001 pad L2: unconnected-(U1001-PadL2) -> (no net)
- U1001 pad L3: unconnected-(U1001-PadL3) -> (no net)
- U1001 pad L4: unconnected-(U1001-PadL4) -> (no net)
- U1001 pad L5: unconnected-(U1001-PadL5) -> (no net)
- U1001 pad L6: unconnected-(U1001-PadL6) -> (no net)
- U1001 pad L7: unconnected-(U1001-PadL7) -> (no net)
- U1001 pad L8: unconnected-(U1001-PadL8) -> (no net)
- U1001 pad L9: unconnected-(U1001-PadL9) -> (no net)
- U1001 pad M1: unconnected-(U1001-PadM1) -> (no net)
- U1001 pad M10: unconnected-(U1001-PadM10) -> (no net)
- U1001 pad M11: unconnected-(U1001-PadM11) -> (no net)
- U1001 pad M12: unconnected-(U1001-PadM12) -> (no net)
- U1001 pad M13: unconnected-(U1001-PadM13) -> (no net)
- U1001 pad M14: unconnected-(U1001-PadM14) -> (no net)
- U1001 pad M15: unconnected-(U1001-PadM15) -> (no net)
- U1001 pad M16: unconnected-(U1001-PadM16) -> (no net)
- U1001 pad M2: unconnected-(U1001-PadM2) -> (no net)
- U1001 pad M3: unconnected-(U1001-PadM3) -> (no net)
- U1001 pad M4: unconnected-(U1001-PadM4) -> (no net)
- U1001 pad M5: unconnected-(U1001-PadM5) -> (no net)
- U1001 pad M6: unconnected-(U1001-PadM6) -> (no net)
- U1001 pad M7: unconnected-(U1001-PadM7) -> (no net)
- U1001 pad M8: unconnected-(U1001-PadM8) -> (no net)
- U1001 pad M9: unconnected-(U1001-PadM9) -> (no net)
- U1001 pad N1: unconnected-(U1001-PadN1) -> (no net)
- U1001 pad N10: unconnected-(U1001-PadN10) -> (no net)
- U1001 pad N11: unconnected-(U1001-PadN11) -> (no net)
- U1001 pad N12: unconnected-(U1001-PadN12) -> (no net)
- U1001 pad N13: unconnected-(U1001-PadN13) -> (no net)
- U1001 pad N14: unconnected-(U1001-PadN14) -> (no net)
- U1001 pad N15: unconnected-(U1001-PadN15) -> (no net)
- U1001 pad N16: unconnected-(U1001-PadN16) -> (no net)
- U1001 pad N2: unconnected-(U1001-PadN2) -> (no net)
- U1001 pad N3: unconnected-(U1001-PadN3) -> (no net)
- U1001 pad N4: unconnected-(U1001-PadN4) -> (no net)
- U1001 pad N5: unconnected-(U1001-PadN5) -> (no net)
- U1001 pad N6: unconnected-(U1001-PadN6) -> (no net)
- U1001 pad N7: unconnected-(U1001-PadN7) -> (no net)
- U1001 pad N8: unconnected-(U1001-PadN8) -> (no net)
- U1001 pad N9: unconnected-(U1001-PadN9) -> (no net)
- U1001 pad P1: unconnected-(U1001-PadP1) -> (no net)
- U1001 pad P10: unconnected-(U1001-PadP10) -> (no net)
- U1001 pad P11: unconnected-(U1001-PadP11) -> (no net)
- U1001 pad P12: unconnected-(U1001-PadP12) -> (no net)
- U1001 pad P13: unconnected-(U1001-PadP13) -> (no net)
- U1001 pad P14: unconnected-(U1001-PadP14) -> (no net)
- U1001 pad P15: unconnected-(U1001-PadP15) -> (no net)
- U1001 pad P16: unconnected-(U1001-PadP16) -> (no net)
- U1001 pad P2: unconnected-(U1001-PadP2) -> (no net)
- U1001 pad P3: unconnected-(U1001-PadP3) -> (no net)
- U1001 pad P4: unconnected-(U1001-PadP4) -> (no net)
- U1001 pad P5: unconnected-(U1001-PadP5) -> (no net)
- U1001 pad P6: unconnected-(U1001-PadP6) -> (no net)
- U1001 pad P7: unconnected-(U1001-PadP7) -> (no net)
- U1001 pad P8: unconnected-(U1001-PadP8) -> (no net)
- U1001 pad P9: unconnected-(U1001-PadP9) -> (no net)
- U1001 pad R1: unconnected-(U1001-PadR1) -> (no net)
- U1001 pad R10: unconnected-(U1001-PadR10) -> (no net)
- U1001 pad R11: unconnected-(U1001-PadR11) -> (no net)
- U1001 pad R12: unconnected-(U1001-PadR12) -> (no net)
- U1001 pad R13: unconnected-(U1001-PadR13) -> (no net)
- U1001 pad R14: unconnected-(U1001-PadR14) -> (no net)
- U1001 pad R15: unconnected-(U1001-PadR15) -> (no net)
- U1001 pad R16: unconnected-(U1001-PadR16) -> (no net)
- U1001 pad R2: unconnected-(U1001-PadR2) -> (no net)
- U1001 pad R3: unconnected-(U1001-PadR3) -> (no net)
- U1001 pad R4: unconnected-(U1001-PadR4) -> (no net)
- U1001 pad R5: unconnected-(U1001-PadR5) -> (no net)
- U1001 pad R6: unconnected-(U1001-PadR6) -> (no net)
- U1001 pad R7: unconnected-(U1001-PadR7) -> (no net)
- U1001 pad R8: unconnected-(U1001-PadR8) -> (no net)
- U1001 pad R9: unconnected-(U1001-PadR9) -> (no net)
- U1001 pad T1: unconnected-(U1001-PadT1) -> (no net)
- U1001 pad T10: unconnected-(U1001-PadT10) -> (no net)
- U1001 pad T11: unconnected-(U1001-PadT11) -> (no net)
- U1001 pad T12: unconnected-(U1001-PadT12) -> (no net)
- U1001 pad T13: unconnected-(U1001-PadT13) -> (no net)
- U1001 pad T14: unconnected-(U1001-PadT14) -> (no net)
- U1001 pad T15: unconnected-(U1001-PadT15) -> (no net)
- U1001 pad T16: unconnected-(U1001-PadT16) -> (no net)
- U1001 pad T2: unconnected-(U1001-PadT2) -> (no net)
- U1001 pad T3: unconnected-(U1001-PadT3) -> (no net)
- U1001 pad T4: unconnected-(U1001-PadT4) -> (no net)
- U1001 pad T5: unconnected-(U1001-PadT5) -> (no net)
- U1001 pad T6: unconnected-(U1001-PadT6) -> (no net)
- U1001 pad T7: unconnected-(U1001-PadT7) -> (no net)
- U1001 pad T8: unconnected-(U1001-PadT8) -> (no net)
- U1001 pad T9: unconnected-(U1001-PadT9) -> (no net)
- U1002 pad A2: unconnected-(U1002-PadA2) -> (no net)
- U1002 pad A3: unconnected-(U1002-PadA3) -> (no net)
- U1002 pad A7: unconnected-(U1002-PadA7) -> (no net)
- U1002 pad B7: unconnected-(U1002-PadB7) -> (no net)
- U1002 pad B8: unconnected-(U1002-PadB8) -> (no net)
- U1002 pad C2: unconnected-(U1002-PadC2) -> (no net)
- U1002 pad C3: unconnected-(U1002-PadC3) -> (no net)
- U1002 pad C7: unconnected-(U1002-PadC7) -> (no net)
- U1002 pad C8: unconnected-(U1002-PadC8) -> (no net)
- U1002 pad D3: unconnected-(U1002-PadD3) -> (no net)
- U1002 pad D7: unconnected-(U1002-PadD7) -> (no net)
- U1002 pad E3: unconnected-(U1002-PadE3) -> (no net)
- U1002 pad E7: unconnected-(U1002-PadE7) -> (no net)
- U1002 pad F2: unconnected-(U1002-PadF2) -> (no net)
- U1002 pad F3: unconnected-(U1002-PadF3) -> (no net)
- U1002 pad F7: unconnected-(U1002-PadF7) -> (no net)
- U1002 pad F8: unconnected-(U1002-PadF8) -> (no net)
- U1002 pad G2: unconnected-(U1002-PadG2) -> (no net)
- U1002 pad G3: unconnected-(U1002-PadG3) -> (no net)
- U1002 pad H1: unconnected-(U1002-PadH1) -> (no net)
- U1002 pad H3: unconnected-(U1002-PadH3) -> (no net)
- U1002 pad H7: unconnected-(U1002-PadH7) -> (no net)
- U1002 pad H8: unconnected-(U1002-PadH8) -> (no net)
- U1002 pad J3: unconnected-(U1002-PadJ3) -> (no net)
- U1002 pad J7: unconnected-(U1002-PadJ7) -> (no net)
- U1002 pad K1: unconnected-(U1002-PadK1) -> (no net)
- U1002 pad K3: unconnected-(U1002-PadK3) -> (no net)
- U1002 pad K7: unconnected-(U1002-PadK7) -> (no net)
- U1002 pad K9: unconnected-(U1002-PadK9) -> (no net)
- U1002 pad L2: unconnected-(U1002-PadL2) -> (no net)
- U1002 pad L3: unconnected-(U1002-PadL3) -> (no net)
- U1002 pad L7: unconnected-(U1002-PadL7) -> (no net)
- U1002 pad L8: unconnected-(U1002-PadL8) -> (no net)
- U1002 pad M2: unconnected-(U1002-PadM2) -> (no net)
- U1002 pad M3: unconnected-(U1002-PadM3) -> (no net)
- U1002 pad M7: unconnected-(U1002-PadM7) -> (no net)
- U1002 pad M8: unconnected-(U1002-PadM8) -> (no net)
- U1002 pad N2: unconnected-(U1002-PadN2) -> (no net)
- U1002 pad N3: unconnected-(U1002-PadN3) -> (no net)
- U1002 pad N7: unconnected-(U1002-PadN7) -> (no net)
- U1002 pad N8: unconnected-(U1002-PadN8) -> (no net)
- U1002 pad P2: unconnected-(U1002-PadP2) -> (no net)
- U1002 pad P3: unconnected-(U1002-PadP3) -> (no net)
- U1002 pad P7: unconnected-(U1002-PadP7) -> (no net)
- U1002 pad P8: unconnected-(U1002-PadP8) -> (no net)
- U1002 pad R2: unconnected-(U1002-PadR2) -> (no net)
- U1002 pad R3: unconnected-(U1002-PadR3) -> (no net)
- U1002 pad R7: unconnected-(U1002-PadR7) -> (no net)
- U1002 pad R8: unconnected-(U1002-PadR8) -> (no net)
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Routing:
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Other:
- board size 227 x 50 mm -> 195.9 x 195.9 mm
- copper layers 2 -> 4
- board text added: "1"
- board text added: "2"
- board text added: "3"
- board text added: "4"
- board text added: "Archer"
- board text added: "Copyright 2021 EI2030"
- board text added: "M2 2242"
- board text added: "R0.1 ES"
